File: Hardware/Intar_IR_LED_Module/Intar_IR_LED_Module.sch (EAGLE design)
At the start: 19 parts, among them J1 GROVE-4P-2.0-3470130P1, Q1 MMBT2222A, Q2 MMBT2222A

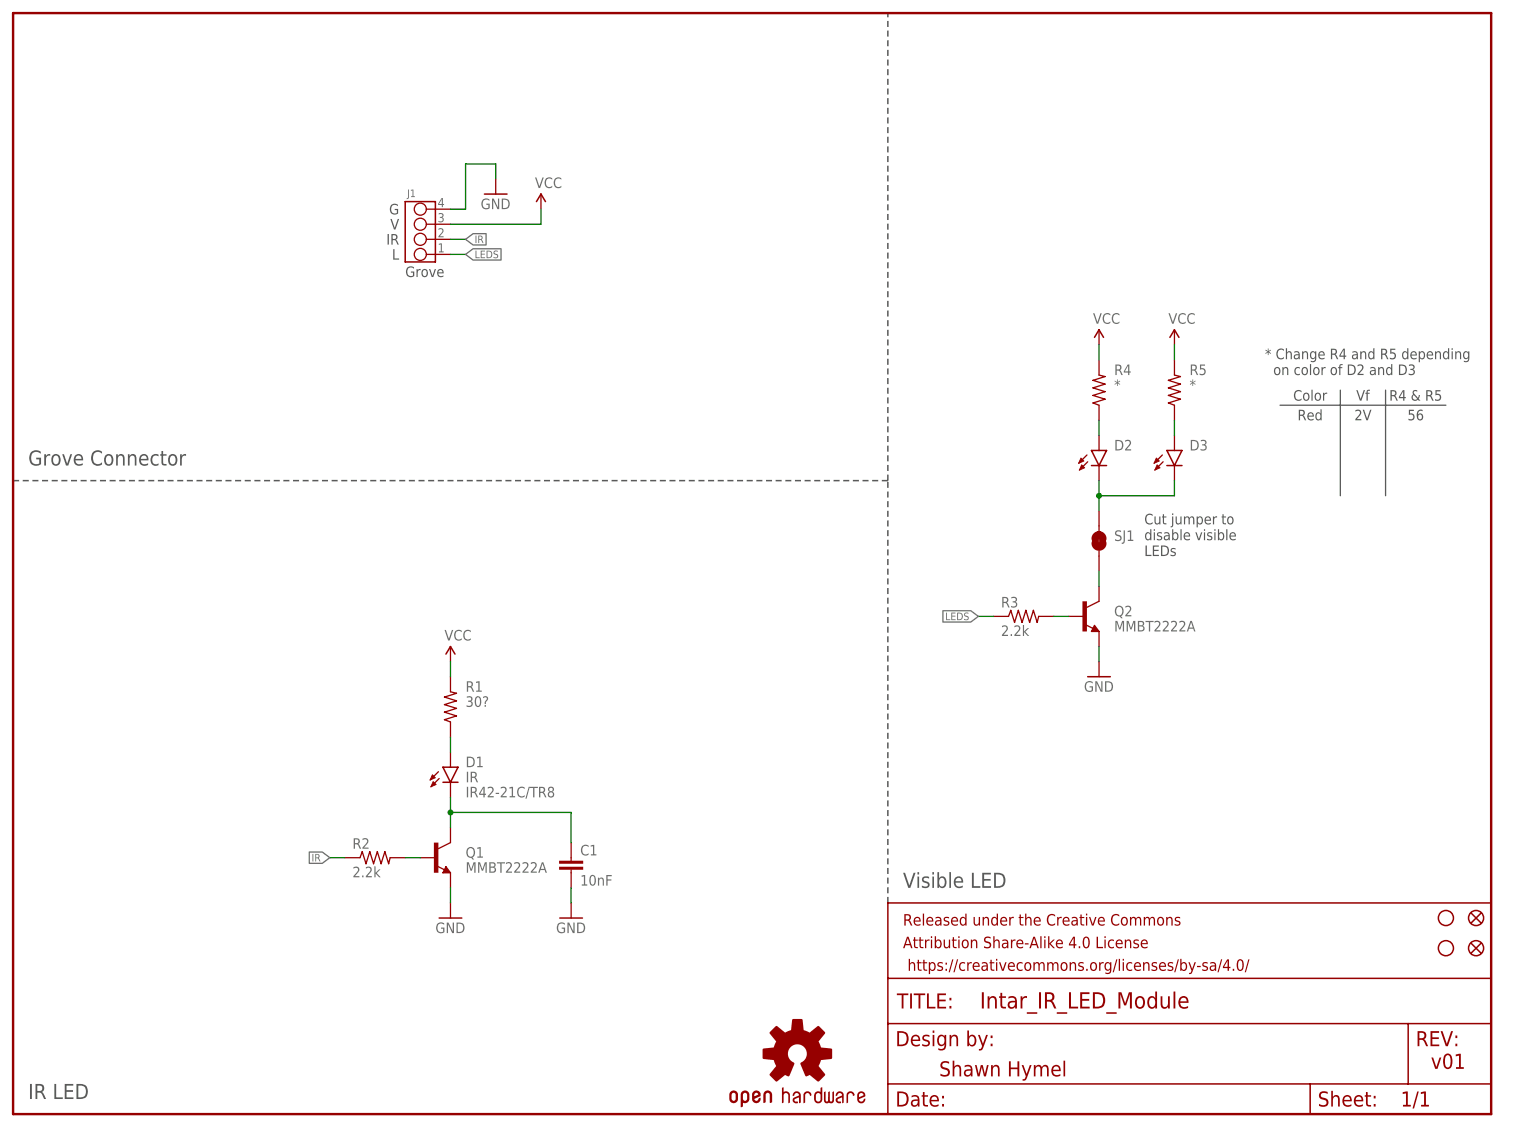
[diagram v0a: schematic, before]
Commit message: Created BOM
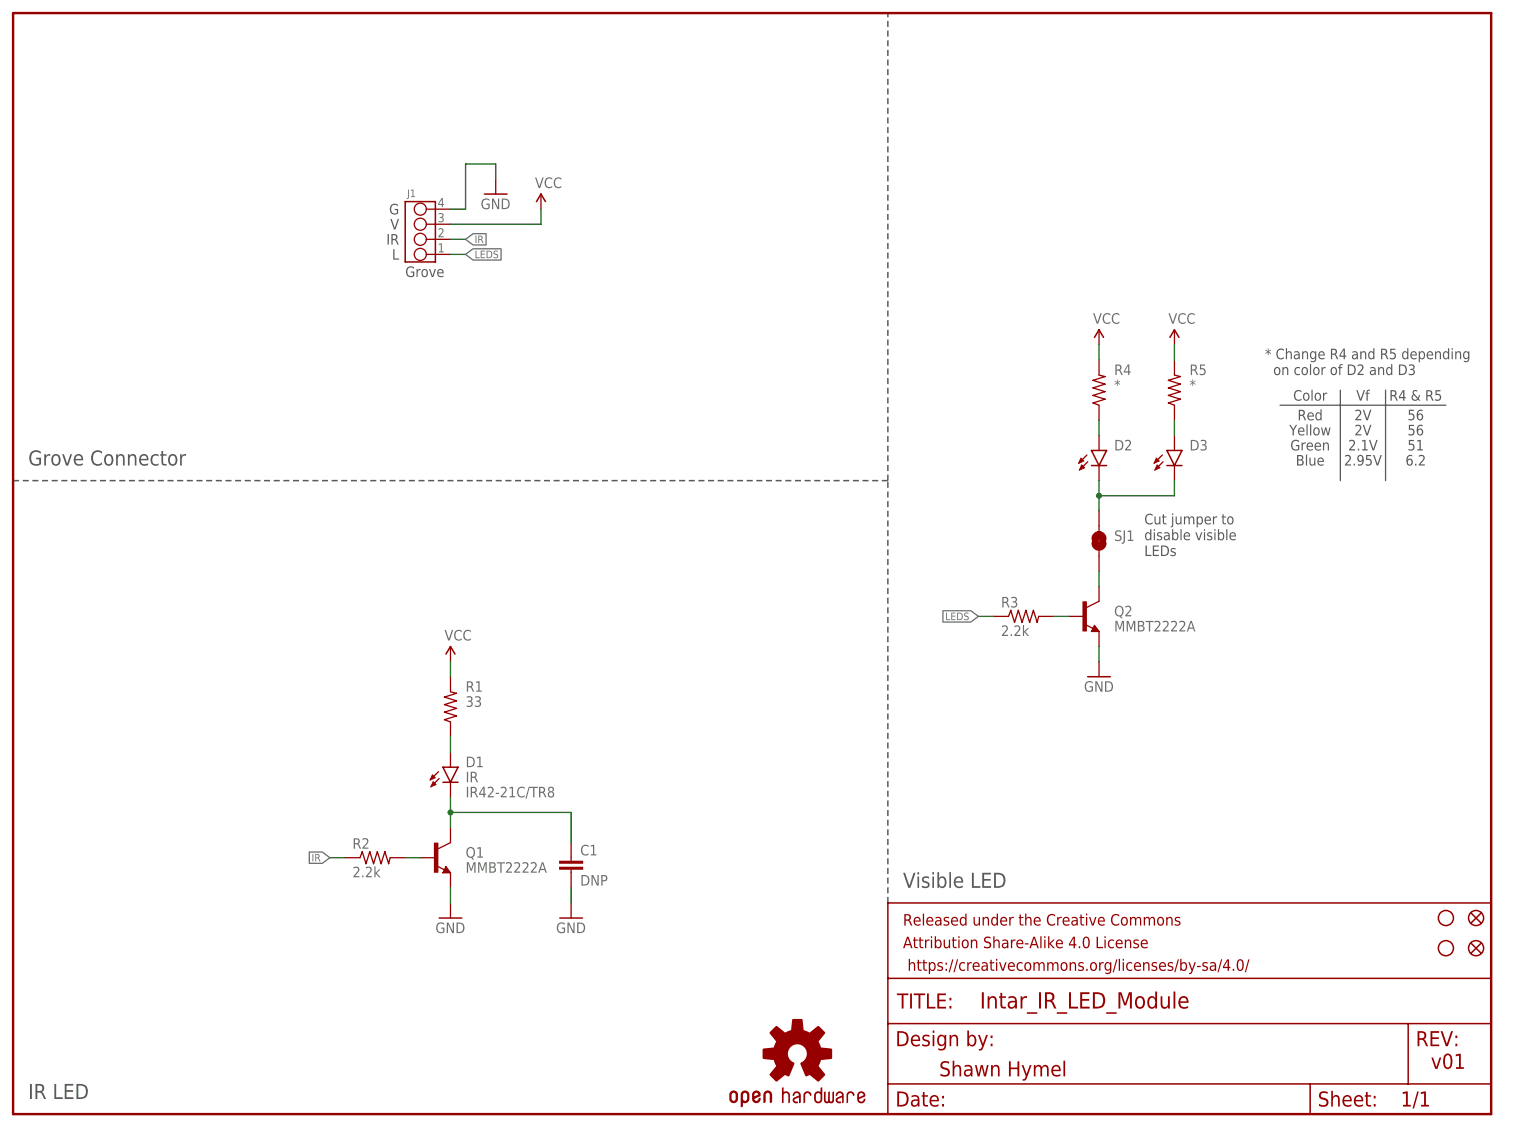
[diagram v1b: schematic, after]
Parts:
- C1: value 10nF -> DNP
- R1: value 30? -> 33
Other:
- note added: "2.1V"
- note added: "2.95V"
- note added: "51"
- note added: "6.2"
- note added: "Blue"
- note added: "Green"
- note added: "Yellow"
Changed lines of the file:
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@@
 <setting verticaltext="up"/>
 </settings>
-<grid distance="0.1" unitdist="inch" unit="inch" style="lines" multiple="1" display="yes" altdistance="0.01" altunitdist="inch" altunit="inch"/>
+<grid distance="0.1" unitdist="inch" unit="inch" style="lines" multiple="1" display="no" altdistance="0.01" altunitdist="inch" altunit="inch"/>
 <layers>
 <layer number="1" name="Top" color="4" fill="1" visible="no" active="no"/>
@@
 <part name="GND1" library="SparkFun-Aesthetics" deviceset="GND" device=""/>
 <part name="SUPPLY1" library="SparkFun-Aesthetics" deviceset="VCC" device=""/>
-<part name="R1" library="SparkFun-Resistors" deviceset="RESISTOR" device="0603-RES" value="30?"/>
+<part name="R1" library="SparkFun-Resistors" deviceset="RESISTOR" device="0603-RES" value="33"/>
 <part name="D1" library="Intar_Eagle_Library" deviceset="LED" device="IR42-21C/TR8" value="IR">
 <attribute name="MFG_NAME" value="IR42-21C/TR8"/>
 </part>
 <part name="Q1" library="SparkFun-DiscreteSemi" deviceset="TRANSISTOR_NPN" device="MMBT2222A" value="MMBT2222A"/>
-<part name="C1" library="SparkFun-Capacitors" deviceset="10NF/10000PF-50V-10%(0603)" device="" value="10nF"/>
+<part name="C1" library="SparkFun-Capacitors" deviceset="10NF/10000PF-50V-10%(0603)" device="" value="DNP"/>
 <part name="SUPPLY2" library="SparkFun-Aesthetics" deviceset="VCC" device=""/>
 <part name="GND2" library="SparkFun-Aesthetics" deviceset="GND" device=""/>
@@
 <text x="236.22" y="120.142" size="1.778" layer="97" align="bottom-center">R4 &amp; R5</text>
 <wire x1="213.36" y1="119.38" x2="241.3" y2="119.38" width="0.1524" layer="97"/>
-<wire x1="223.52" y1="121.92" x2="223.52" y2="104.14" width="0.1524" layer="97"/>
-<wire x1="231.14" y1="121.92" x2="231.14" y2="104.14" width="0.1524" layer="97"/>
+<wire x1="223.52" y1="121.92" x2="223.52" y2="106.68" width="0.1524" layer="97"/>
+<wire x1="231.14" y1="121.92" x2="231.14" y2="106.68" width="0.1524" layer="97"/>
 <text x="218.44" y="116.84" size="1.778" layer="97" align="bottom-center">Red</text>
 <text x="227.33" y="116.84" size="1.778" layer="97" align="bottom-center">2V</text>
@@
 <text x="65.024" y="147.32" size="1.778" layer="97" align="center-right">IR</text>
 <text x="65.024" y="144.78" size="1.778" layer="97" align="center-right">L</text>
+<text x="218.44" y="114.3" size="1.778" layer="97" align="bottom-center">Yellow</text>
+<text x="227.33" y="114.3" size="1.778" layer="97" align="bottom-center">2V</text>
+<text x="236.22" y="114.3" size="1.778" layer="97" align="bottom-center">56</text>
+<text x="218.44" y="111.76" size="1.778" layer="97" align="bottom-center">Green</text>
+<text x="227.33" y="111.76" size="1.778" layer="97" align="bottom-center">2.1V</text>
+<text x="236.22" y="111.76" size="1.778" layer="97" align="bottom-center">51</text>
+<text x="218.44" y="109.22" size="1.778" layer="97" align="bottom-center">Blue</text>
+<text x="227.33" y="109.22" size="1.778" layer="97" align="bottom-center">2.95V</text>
+<text x="236.22" y="109.22" size="1.778" layer="97" align="bottom-center">6.2</text>
 </plain>
 <instances>
